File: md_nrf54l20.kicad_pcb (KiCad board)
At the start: 2 copper layers, 68.6 x 53.3 mm, 8 parts, among them J1 Power, J2 Digital/PWM, J3 Analog, J4 Digital/PWM

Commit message: Update layout
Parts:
- added C1: 10uF, Capacitor_SMD:C_0805_2012Metric, F.Cu at (117.8, 80.0)
- added C10: 22uF, Capacitor_SMD:C_0805_2012Metric, F.Cu at (115.3, 80.0)
- added C11: 100nF, Capacitor_SMD:C_0603_1608Metric, F.Cu at (113.5, 79.9)
- added C12: 22pF, Capacitor_SMD:C_0603_1608Metric, F.Cu at (118.7, 66.5)
- added C13: 22pF, Capacitor_SMD:C_0603_1608Metric, F.Cu at (118.7, 69.6)
- added C14: 100nF, Capacitor_SMD:C_0603_1608Metric, F.Cu at (119.8, 62.4)
- added C15: 1uF, Capacitor_SMD:C_0603_1608Metric, F.Cu at (118.2, 62.4)
- added C16: 100nF, Capacitor_SMD:C_0603_1608Metric, F.Cu at (132.9, 89.0)
- added C2: 100nF, Capacitor_SMD:C_0603_1608Metric, F.Cu at (135.6, 83.0)
- added C3: 100nF, Capacitor_SMD:C_0603_1608Metric, F.Cu at (130.7, 83.2)
- added C4: 100nF, Capacitor_SMD:C_0603_1608Metric, F.Cu at (137.9, 78.7)
- added C5: 2.2uF, Capacitor_SMD:C_0603_1608Metric, F.Cu at (129.6, 85.8)
- added C6: 4.7uF, Capacitor_SMD:C_0603_1608Metric, F.Cu at (134.5, 85.9)
- added C7: 12pF, Capacitor_SMD:C_0603_1608Metric, F.Cu at (127.1, 78.6)
- added C8: 12pF, Capacitor_SMD:C_0603_1608Metric, F.Cu at (127.1, 81.7)
- added C9: 10uF, Capacitor_SMD:C_0805_2012Metric, F.Cu at (107.3, 82.5)
- added FB1: 120R@100MHz, Inductor_SMD:L_0603_1608Metric, F.Cu at (132.9, 87.4)
- added J5: USB_C, Connector_USB:USB_C_Receptacle_HRO_TYPE-C-31-M-12, F.Cu at (102.6, 61.7)
- added J6: USB_C, Connector_USB:USB_C_Receptacle_HRO_TYPE-C-31-M-12, F.Cu at (102.6, 92.4)
- added L1: 4.7uH, Inductor_SMD:L_0603_1608Metric, F.Cu at (132.4, 83.2)
- added R1: 10k, Resistor_SMD:R_0603_1608Metric, F.Cu at (125.1, 74.3)
- added R2: 5.1k, Resistor_SMD:R_0603_1608Metric, F.Cu at (109.7, 59.6)
- added R3: 5.1k, Resistor_SMD:R_0603_1608Metric, F.Cu at (109.8, 63.4)
- added R4: 5.1k, Resistor_SMD:R_0603_1608Metric, F.Cu at (109.4, 91.2)
- added R5: 5.1k, Resistor_SMD:R_0603_1608Metric, F.Cu at (109.4, 94.1)
- added U1: nRF54L20, md_nrf54l20:QFN-52-1EP_6x6mm_P0.4mm_EP4.7x4.7mm, F.Cu at (132.9, 77.8)
- added U2: AMS1117-3.3, Package_TO_SOT_SMD:SOT-89-3, F.Cu at (110.4, 78.9)
- added U3: CH347T, Package_SO:TSSOP-20_4.4x6.5mm_P0.65mm, F.Cu at (124.7, 65.8)
- added Y1: 8MHz, Crystal:Crystal_SMD_3225-4Pin_3.2x2.5mm, F.Cu at (115.5, 67.9)
- added Y2: 32MHz, Crystal:Crystal_SMD_3225-4Pin_3.2x2.5mm, F.Cu at (124.5, 79.8)
- J1: value Power -> POWER
- J2: value Digital/PWM -> DIGITAL_8_13
- J3: value Analog -> ANALOG
- J4: value Digital/PWM -> DIGITAL_0_7
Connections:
- net /SCL/A5 renamed /A5_SCL
- net /SDA/A4 renamed /A4_SDA
- J1 pad 2: /IOREF -> +3V3
- J1 pad 3: /~{RESET} -> /nRESET
- J1 pad 5: +5V -> VBUS
- J1 pad 8: VCC -> unconnected-(J1-Pin_8-Pad8)
- J2 pad 10: /8 -> /D8
- J2 pad 5: /13 -> /D13_SCK
- J2 pad 6: /12 -> /D12_CITO
- J2 pad 7: /*11 -> /D11_COTI
- J2 pad 8: /*10 -> /D10_CS
- J2 pad 9: /*9 -> /D9_PWM
- J4 pad 1: /7 -> /D7
- J4 pad 2: /*6 -> /D6_PWM
- J4 pad 3: /*5 -> /D5_PWM
- J4 pad 4: /4 -> /D4
- J4 pad 5: /*3 -> /D3_PWM
- J4 pad 6: /2 -> /D2
- J4 pad 7: /TX/1 -> /D1_TX
- J4 pad 8: /RX/0 -> /D0_RX
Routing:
- net VBUS: track 0.00 -> 70.9 mm
- net /USB_DN: track 0.00 -> 54.5 mm
- net /USB_DP: track 0.00 -> 53.0 mm
- net /D9_PWM: track 0.00 -> 50.1 mm, vias 0 -> 2
- net /D10_CS: track 0.00 -> 48.5 mm, vias 0 -> 2
- net /D11_COTI: track 0.00 -> 48.0 mm, vias 0 -> 2
- net /D0_RX: track 0.00 -> 47.4 mm
- net /D1_TX: track 0.00 -> 45.4 mm
- net /D2: track 0.00 -> 43.0 mm
- net /D12_CITO: track 0.00 -> 42.2 mm, vias 0 -> 1
- net /D3_PWM: track 0.00 -> 41.7 mm
- net /D13_SCK: track 0.00 -> 41.4 mm, vias 0 -> 1
- net /D4: track 0.00 -> 40.4 mm
- net /D5_PWM: track 0.00 -> 39.0 mm
- net /D6_PWM: track 0.00 -> 37.6 mm
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- added copper zone on In2.Cu, net +3V3
- added copper zone on B.Cu, net GND
- added copper zone on F.Cu, net GND
- added copper zone on In1.Cu, net GND
- added copper zone on In2.Cu, net GND
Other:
- copper layers 2 -> 4

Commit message: Update layout
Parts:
- added D1: R_LED, LED_SMD:LED_0805_2012Metric, F.Cu at (153.9, 59.9)
- added D2: O_LED, LED_SMD:LED_0805_2012Metric, F.Cu at (127.3, 59.9)
- added D3: G_LED, LED_SMD:LED_0805_2012Metric, F.Cu at (153.9, 63.6)
- added R6: 470, Resistor_SMD:R_0603_1608Metric, F.Cu at (153.9, 58.0)
- added R7: 330, Resistor_SMD:R_0603_1608Metric, F.Cu at (125.3, 59.9)
- added R8: 220, Resistor_SMD:R_0603_1608Metric, F.Cu at (153.9, 61.7)
- added SW1: RESET, md_nrf54l20:micro-switch, F.Cu at (105.8, 51.5)
- moved R5 2.95 mm to (109.4, 91.2)
- moved R4 2.80 mm to (109.4, 94.0)
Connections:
- U1 pad 52: unconnected-(U1-P2.00-Pad52) -> Net-(D3-A)
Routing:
- net /A5_SCL: track 0.00 -> 84.9 mm, vias 0 -> 1
- net /A4_SDA: track 0.00 -> 79.2 mm, vias 0 -> 1
- net Net-(D3-A): track 0.00 -> 27.2 mm, vias 0 -> 2
- net +3V3: track 25.5 -> 35.8 mm, vias 6 -> 12
- net /UART_RX: track 11.2 -> 19.6 mm
- net Net-(D1-K): track 0.00 -> 2.42 mm
- net Net-(D2-K): track 0.00 -> 1.99 mm
- net Net-(D3-K): track 0.00 -> 1.93 mm
- net Net-(U1-DECRF): track 26.3 -> 27.8 mm
- net VBUS: track 70.9 -> 70.0 mm
- net GND: vias 1 -> 8

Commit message: Update layout
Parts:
- added J7: Conn_01x04, Connectors_JST:JST_SH_SM04B-SRSS-TB_04x1.00mm_Angled, F.Cu at (160.2, 72.1)
- moved C2 1.21 mm to (136.8, 82.9)
- moved L1 0.78 mm to (132.2, 84.0)
- moved C6 0.61 mm to (135.1, 85.8)
- moved C3 0.07 mm to (130.6, 83.3)
- turned R6 to 0 degrees
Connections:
- SW1 pad 1: (no net) -> /nRESET
- SW1 pad 2: (no net) -> GND
- U1 pad 48: unconnected-(U1-P1.20-Pad48) -> Net-(J7-Pin_3)
- U1 pad 49: unconnected-(U1-P1.21-Pad49) -> Net-(J7-Pin_4)
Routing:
- net /nRESET: track 37.3 -> 71.3 mm, vias 0 -> 2
- net Net-(J7-Pin_3): track 0.00 -> 32.7 mm, vias 0 -> 2
- net Net-(J7-Pin_4): track 0.00 -> 32.7 mm, vias 0 -> 2
- net /D12_CITO: track 42.2 -> 43.3 mm
- net /D11_COTI: track 48.0 -> 49.2 mm
- net GND: track 0.00 -> 1.06 mm, vias 8 -> 11
- net /D10_CS: track 48.5 -> 49.4 mm
- net /D9_PWM: track 50.1 -> 51.0 mm
- net /D13_SCK: track 41.4 -> 42.2 mm
- net +3V3: track 35.8 -> 36.6 mm

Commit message: Update layout
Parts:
- removed J1: POWER, Connector_PinSocket_2.54mm:PinSocket_1x08_P2.54mm_Vertical
- removed J2: DIGITAL_8_13, Connector_PinSocket_2.54mm:PinSocket_1x10_P2.54mm_Vertical
- removed J3: ANALOG, Connector_PinSocket_2.54mm:PinSocket_1x06_P2.54mm_Vertical
- removed J4: DIGITAL_0_7, Connector_PinSocket_2.54mm:PinSocket_1x08_P2.54mm_Vertical
- removed J6: USB_C, Connector_USB:USB_C_Receptacle_HRO_TYPE-C-31-M-12
- removed R4, R5: 5.1k, Resistor_SMD:R_0603_1608Metric
- removed SW1: RESET, md_nrf54l20:micro-switch
- added J10: Conn_01x15, Connector_PinHeader_2.54mm:PinHeader_1x15_P2.54mm_Vertical, B.Cu at (103.8, 83.5)
- added J9: Conn_01x15, Connector_PinHeader_2.54mm:PinHeader_1x15_P2.54mm_Vertical, B.Cu at (103.8, 98.7)
- added R10: 10k, Resistor_SMD:R_0603_1608Metric, F.Cu at (122.6, 70.5)
- added R9: 10k, Resistor_SMD:R_0603_1608Metric, F.Cu at (122.6, 68.0)
- added U4: M6017-02, md_nrf54l20:SIM-SMD_M6017-02, F.Cu at (140.2, 91.0)
- MH1, MH2, MH3, MH4: value MountingHole_3.2mm -> MountingHole_65mil; footprint Arduino_MountingHole:MountingHole_3.2mm -> Arduino_MountingHole:MountingHole_65mil
- moved MH1 51.5 mm to (101.3, 98.7)
- moved J7 35.9 mm to (131.2, 93.3), turned to 0 degrees
- moved C2 35.3 mm to (114.6, 55.5), turned to 0 degrees
- moved R8 31.5 mm to (122.6, 65.5), turned to 0 degrees
- moved R6 31.4 mm to (122.6, 60.5)
- moved MH3 30.7 mm to (141.9, 83.5)
- moved C3 29.9 mm to (114.6, 58.0), turned to 0 degrees
- moved C4 29.6 mm to (114.6, 60.5)
- moved J5 29.1 mm to (102.1, 90.8)
- moved C9 29.1 mm to (134.8, 72.9), turned to 0 degrees
- moved C6 28.8 mm to (114.6, 65.5)
- moved C16 27.5 mm to (118.6, 65.5)
- moved C5 27.3 mm to (114.6, 63.0), turned to 0 degrees
- moved U3 26.7 mm to (111.4, 88.9)
- moved MH4 25.0 mm to (141.9, 98.7)
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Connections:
- J7 pad 1: unconnected-(J7-Pin_1-Pad1) -> GND
- J7 pad 2: unconnected-(J7-Pin_2-Pad2) -> +3V3
- J7 pad 3: Net-(J7-Pin_3) -> unconnected-(J7-Pin_3-Pad3)
- J7 pad 4: Net-(J7-Pin_4) -> unconnected-(J7-Pin_4-Pad4)
- U1 pad 11: /D7 -> /A1
- U1 pad 12: /D8 -> /A2
- U1 pad 13: /A5_SCL -> /A3
- U1 pad 16: /A4_SDA -> unconnected-(U1-P1.06-Pad16)
- U1 pad 22: /AREF -> unconnected-(U1-P1.07-Pad22)
- U1 pad 23: /D0_RX -> unconnected-(U1-P1.08-Pad23)
- U1 pad 24: /D1_TX -> unconnected-(U1-P1.09-Pad24)
- U1 pad 39: /D9_PWM -> unconnected-(U1-P1.15-Pad39)
- U1 pad 40: /D10_CS -> unconnected-(U1-P1.16-Pad40)
- U1 pad 41: /D11_COTI -> unconnected-(U1-P1.18-Pad41)
- U1 pad 47: /D12_CITO -> unconnected-(U1-P1.19-Pad47)
- U1 pad 48: Net-(J7-Pin_3) -> unconnected-(U1-P1.20-Pad48)
- U1 pad 49: Net-(J7-Pin_4) -> unconnected-(U1-P1.21-Pad49)
- U1 pad 50: /D13_SCK -> unconnected-(U1-P1.24-Pad50)
- U1 pad 7: /A0 -> unconnected-(U1-P1.29-Pad7)
- U1 pad 8: /A1 -> unconnected-(U1-P1.30-Pad8)
- U1 pad 9: /A2 -> unconnected-(U1-P1.31-Pad9)
- U3 pad 10: unconnected-(U3-DTR1/MODE0-Pad10) -> /MODE_D
- U3 pad 13: unconnected-(U3-RTS1/MODE1-Pad13) -> /MODE_R
- U3 pad 5: unconnected-(U3-SCS0/TMS-Pad5) -> /SWDIO
- U3 pad 6: unconnected-(U3-SCK/TCK-Pad6) -> /SWDCLK
- U3 pad 9: unconnected-(U3-SCS1/TRST-Pad9) -> /nRESET
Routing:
- net /A5_SCL: track 84.9 -> 0.00 mm, vias 1 -> 0
- net /A4_SDA: track 79.2 -> 0.00 mm, vias 1 -> 0
- net /nRESET: track 71.3 -> 0.00 mm, vias 2 -> 0
- net VBUS: track 70.0 -> 0.00 mm
- net /USB_DN: track 54.5 -> 0.00 mm
- net /USB_DP: track 53.0 -> 0.00 mm
- net /D9_PWM: track 51.0 -> 0.00 mm, vias 2 -> 0
- net /D10_CS: track 49.4 -> 0.00 mm, vias 2 -> 0
- net /D11_COTI: track 49.2 -> 0.00 mm, vias 2 -> 0
- net /D0_RX: track 47.4 -> 0.00 mm
- net /D1_TX: track 45.4 -> 0.00 mm
- net /D12_CITO: track 43.3 -> 0.00 mm, vias 1 -> 0
- net /D2: track 43.0 -> 0.00 mm
- net /D13_SCK: track 42.2 -> 0.00 mm, vias 1 -> 0
- net /D3_PWM: track 41.7 -> 0.00 mm
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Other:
- board size 68.6 x 53.3 mm -> 43.2 x 17.8 mm
- board text added: "USB-C"

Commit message: Update layout
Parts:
- moved C9 14.3 mm to (143.8, 61.9)
- moved C1 14.3 mm to (143.8, 58.9)
- moved C10 14.3 mm to (143.8, 64.9)
- moved D1 14.3 mm to (148.3, 58.9)
- moved D3 14.3 mm to (148.3, 65.0)
- moved D2 14.3 mm to (148.3, 61.9)
- moved Y1 9.76 mm to (133.4, 61.5)
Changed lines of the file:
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@@
 		(capping no)
 		(filling no)
+		(zone_defaults)
 		(aux_axis_origin 100 100)
 		(grid_origin 100 100)
@@
 	(footprint "Capacitor_SMD:C_0805_2012Metric"
 		(layer "F.Cu")
-		(at 134.75 75.91)
+		(at 143.85 64.91)
 		(descr "Capacitor SMD 0805 (2012 Metric), square (rectangular) end terminal, IPC-7351 nominal, (Body size source: IPC-SM-782 page 76, https://www.pcb-3d.com/wordpress/wp-content/uploads/ipc-sm-782a_amendment_1_and_2.pdf, https://docs.google.com/spreadsheets/d/1BsfQQcO9C6DZCsRaXUlFlo91Tg2WpOkGARC1WS5S8t0/edit?usp=sharing)")
 		(tags "capacitor")
@@
 	(footprint "LED_SMD:LED_0805_2012Metric"
 		(layer "F.Cu")
-		(at 139.22 69.905)
+		(at 148.32 58.905)
 		(descr "LED SMD 0805 (2012 Metric), square (rectangular) end terminal, IPC-7351 nominal, (Body size source: https://docs.google.com/spreadsheets/d/1BsfQQcO9C6DZCsRaXUlFlo91Tg2WpOkGARC1WS5S8t0/edit?usp=sharing)")
 		(tags "LED")
@@
 	(footprint "Capacitor_SMD:C_0805_2012Metric"
 		(layer "F.Cu")
-		(at 134.75 72.9)
+		(at 143.85 61.9)
 		(descr "Capacitor SMD 0805 (2012 Metric), square (rectangular) end terminal, IPC-7351 nominal, (Body size source: IPC-SM-782 page 76, https://www.pcb-3d.com/wordpress/wp-content/uploads/ipc-sm-782a_amendment_1_and_2.pdf, https://docs.google.com/spreadsheets/d/1BsfQQcO9C6DZCsRaXUlFlo91Tg2WpOkGARC1WS5S8t0/edit?usp=sharing)")
 		(tags "capacitor")
@@
 	(footprint "LED_SMD:LED_0805_2012Metric"
 		(layer "F.Cu")
-		(at 139.22 75.985)
+		(at 148.32 64.985)
 		(descr "LED SMD 0805 (2012 Metric), square (rectangular) end terminal, IPC-7351 nominal, (Body size source: https://docs.google.com/spreadsheets/d/1BsfQQcO9C6DZCsRaXUlFlo91Tg2WpOkGARC1WS5S8t0/edit?usp=sharing)")
 		(tags "LED")
@@
 	(footprint "LED_SMD:LED_0805_2012Metric"
 		(layer "F.Cu")
-		(at 139.22 72.945)
+		(at 148.32 61.945)
 		(descr "LED SMD 0805 (2012 Metric), square (rectangular) end terminal, IPC-7351 nominal, (Body size source: https://docs.google.com/spreadsheets/d/1BsfQQcO9C6DZCsRaXUlFlo91Tg2WpOkGARC1WS5S8t0/edit?usp=sharing)")
 		(tags "LED")
@@
 	(footprint "Crystal:Crystal_SMD_3225-4Pin_3.2x2.5mm"
 		(layer "F.Cu")
-		(at 129.9 70.66)
+		(at 133.4 61.55)
 		(descr "SMD3225/4, Crystal, 3.2x2.5mm package, SMD, http://www.txccrystal.com/images/pdf/7m-accuracy.pdf")
 		(property "Reference" "Y1"
-			(at 0 -2.45 0)
+			(at 0 -2.5 0)
 			(layer "F.SilkS")
 			(effects
@@
 		)
 		(fp_text user "${REFERENCE}"
-			(at 0 0 0)
+			(at 0 -0.05 0)
 			(layer "F.Fab")
 			(effects
@@
 	(footprint "Capacitor_SMD:C_0805_2012Metric"
 		(layer "F.Cu")
-		(at 134.75 69.89)
+		(at 143.85 58.89)
 		(descr "Capacitor SMD 0805 (2012 Metric), square (rectangular) end terminal, IPC-7351 nominal, (Body size source: IPC-SM-782 page 76, https://www.pcb-3d.com/wordpress/wp-content/uploads/ipc-sm-782a_amendment_1_and_2.pdf, https://docs.google.com/spreadsheets/d/1BsfQQcO9C6DZCsRaXUlFlo91Tg2WpOkGARC1WS5S8t0/edit?usp=sharing)")
 		(tags "capacitor")
@@
 				(font
 					(size 1.27 1.27)
+					(thickness 0.15)
 				)
 			)
@@
 				(font
 					(size 1.27 1.27)
+					(thickness 0.15)
 				)
 			)

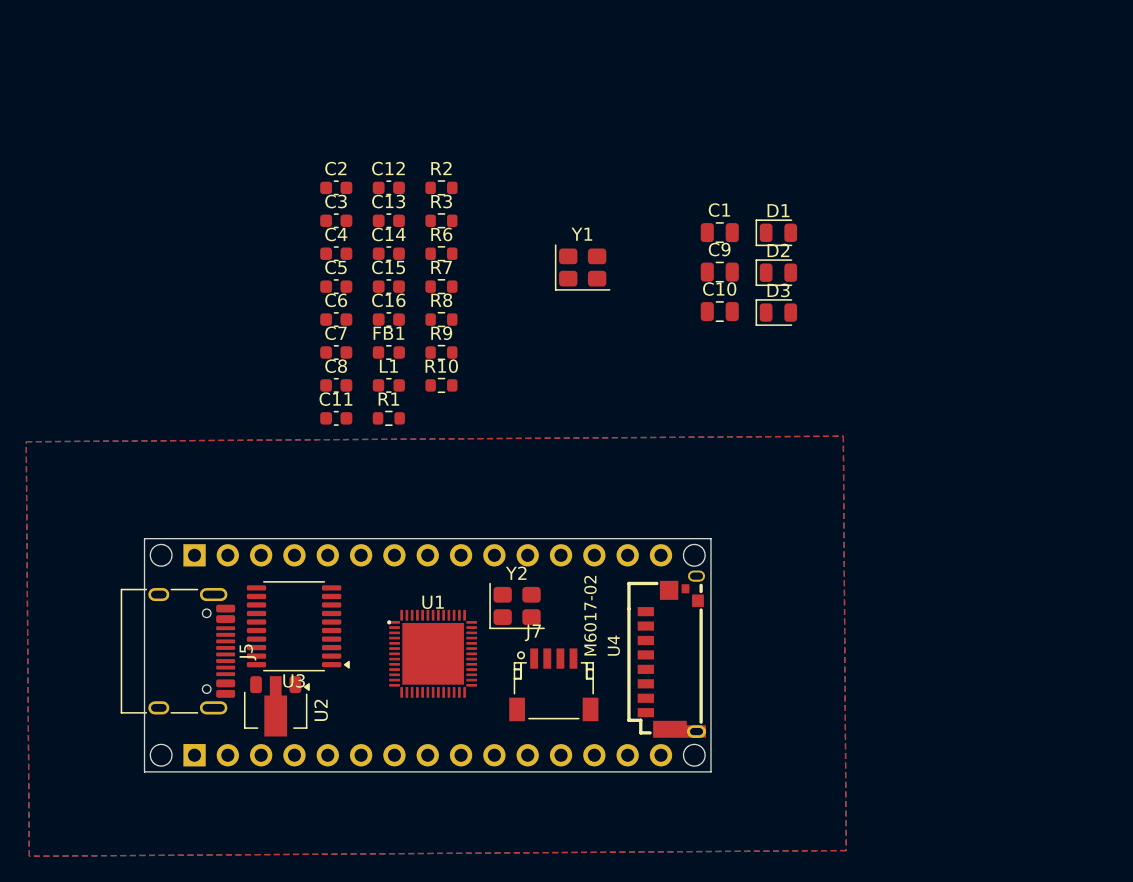
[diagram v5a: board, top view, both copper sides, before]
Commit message: Fix nets in schematic
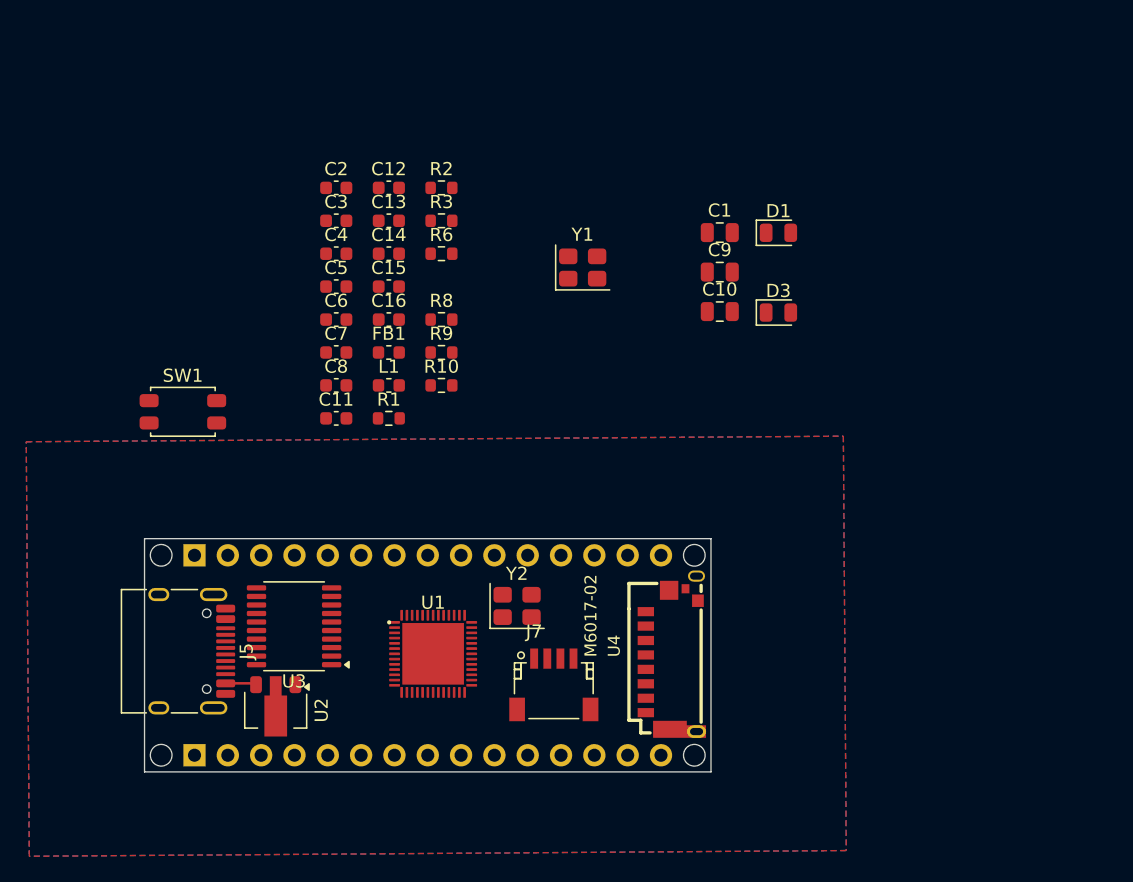
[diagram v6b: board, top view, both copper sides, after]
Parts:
- removed D2: O_LED, LED_SMD:LED_0805_2012Metric
- removed R7: 330, Resistor_SMD:R_0603_1608Metric
- added SW1: RESET, Button_Switch_SMD:SW_SPST_EVQP2_MiddlePushTravel_H2.5mm, F.Cu at (102.9, 72.5)
- J7: value Conn_01x04 -> JST SH I2C
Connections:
- net Net-(D3-A) renamed /USER_LED
- J7 pad 3: unconnected-(J7-Pin_3-Pad3) -> /QWIIC_SDA
- J7 pad 4: unconnected-(J7-Pin_4-Pad4) -> /QWIIC_SCL
- U1 pad 1: unconnected-(U1-P2.01-Pad1) -> /SD_CS
- U1 pad 10: /A3 -> /A0
- U1 pad 11: /A1 -> unconnected-(U1-P1.01-Pad11)
- U1 pad 12: /A2 -> unconnected-(U1-P1.02-Pad12)
- U1 pad 13: /A3 -> /D8
- U1 pad 14: /UART_TX -> /D7
- U1 pad 15: /UART_RX -> /A5_SCL
- U1 pad 16: unconnected-(U1-P1.06-Pad16) -> /A4_SDA
- U1 pad 2: unconnected-(U1-P2.02-Pad2) -> /SD_MOSI
- U1 pad 22: unconnected-(U1-P1.07-Pad22) -> /D6_PWM
- U1 pad 23: unconnected-(U1-P1.08-Pad23) -> /D5_PWM
- U1 pad 24: unconnected-(U1-P1.09-Pad24) -> /D4
- U1 pad 26: /D2 -> /D13_SCK
- U1 pad 27: /D3_PWM -> /D12_CITO
- U1 pad 28: /D4 -> /D11_COTI
- U1 pad 29: /D5_PWM -> /D10_CS
- U1 pad 30: /D6_PWM -> /D9_PWM
- U1 pad 39: unconnected-(U1-P1.15-Pad39) -> /D3_PWM
- U1 pad 4: unconnected-(U1-P2.04-Pad4) -> /SD_MISO
- U1 pad 40: unconnected-(U1-P1.16-Pad40) -> /D2
- U1 pad 41: unconnected-(U1-P1.18-Pad41) -> /D1_TX
- U1 pad 47: unconnected-(U1-P1.19-Pad47) -> /D0_RX
- U1 pad 48: unconnected-(U1-P1.20-Pad48) -> /QWIIC_SDA
- U1 pad 49: unconnected-(U1-P1.21-Pad49) -> /QWIIC_SCL
- U1 pad 5: unconnected-(U1-P2.05-Pad5) -> /SD_SCK
- U1 pad 7: unconnected-(U1-P1.29-Pad7) -> /A3
- U1 pad 8: unconnected-(U1-P1.30-Pad8) -> /A2
- U1 pad 9: unconnected-(U1-P1.31-Pad9) -> /A1
- U3 pad 3: /UART_RX -> unconnected-(U3-TXD1-Pad3)
- U3 pad 4: /UART_TX -> unconnected-(U3-RXD1-Pad4)
- U4 pad EH: unconnected-(U4-PadEH) -> GND
- U4 pad P2: unconnected-(U4-CD/D3-PadP2) -> /SD_CS
- U4 pad P3: unconnected-(U4-CMD-PadP3) -> /SD_MOSI
- U4 pad P4: unconnected-(U4-VDD-PadP4) -> +3V3
- U4 pad P5: unconnected-(U4-CLK-PadP5) -> /SD_SCK
- U4 pad P6: unconnected-(U4-VSS-PadP6) -> GND
- U4 pad P7: unconnected-(U4-D0-PadP7) -> /SD_MISO
- U4 pad SHELL: unconnected-(U4-PadSHELL) -> GND
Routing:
- net VBUS: track 0.00 -> 2.36 mm

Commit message: Add caps to pcb
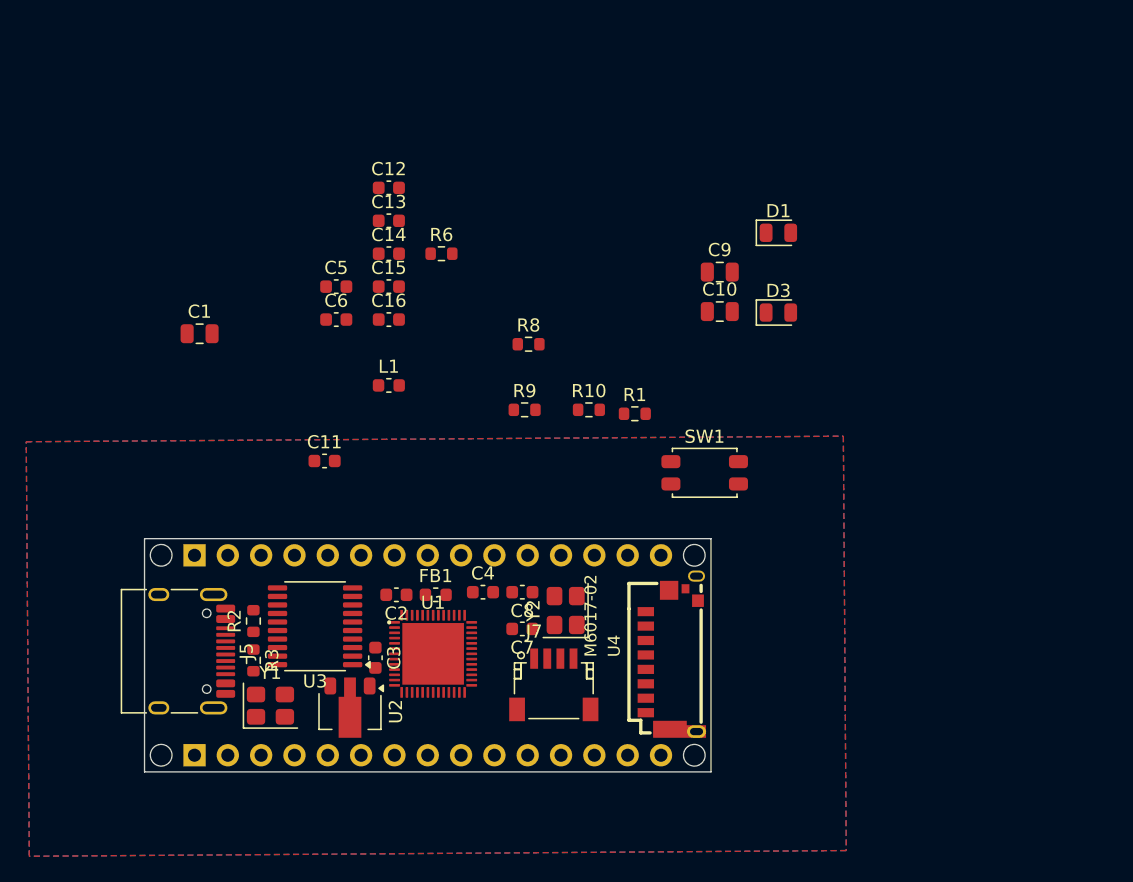
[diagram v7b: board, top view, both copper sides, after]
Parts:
- moved Y1 41.0 mm to (109.6, 95.0)
- moved C1 40.4 mm to (104.2, 66.6)
- moved SW1 40.0 mm to (142.7, 77.2)
- moved R3 36.4 mm to (108.3, 91.5), turned to -90 degrees
- moved R2 36.0 mm to (108.3, 88.5), turned to 90 degrees
- moved C3 33.4 mm to (117.6, 91.3), turned to -90 degrees
- moved C2 31.4 mm to (119.2, 86.5), turned to 180 degrees
- moved C4 28.1 mm to (125.8, 86.3)
- moved C7 25.4 mm to (128.8, 89.1), turned to 180 degrees
- moved C8 21.2 mm to (128.8, 86.3), turned to 180 degrees
- moved FB1 18.8 mm to (122.2, 86.5)
- moved R1 18.8 mm to (137.4, 72.7)
- moved R10 11.4 mm to (133.9, 72.4)
- moved R9 7.70 mm to (129.0, 72.4)
- moved R8 6.90 mm to (129.3, 67.4)
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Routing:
- net VBUS: track 2.36 -> 0.00 mm
